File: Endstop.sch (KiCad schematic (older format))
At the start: 4 parts

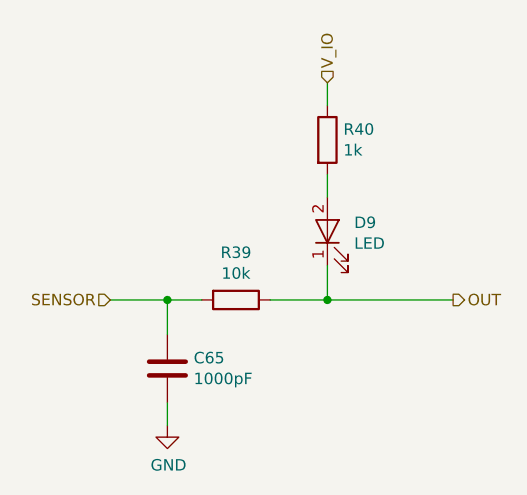
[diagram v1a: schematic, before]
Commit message: Finish the schematics. All pins are assinged to the NUCLEO-64 board.
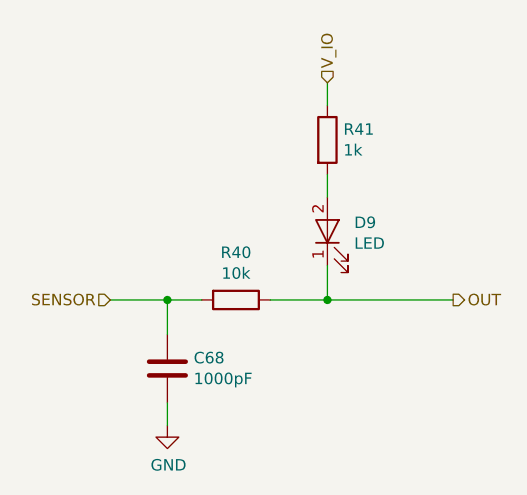
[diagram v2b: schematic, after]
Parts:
- renumbered C12 to C15, R5 to R6, R6 to R7
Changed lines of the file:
@@
 $Descr A4 11693 8268
 encoding utf-8
-Sheet 10 35
+Sheet 5 35
 Title ""
 Date ""
@@
 $EndDescr
 $Comp
-L Device:R R5
+L Device:R R6
 U 1 1 5ACC8647
 P 3950 2850
-AR Path="/5AC337B6/5ACBE919/5AD4BBBB/5ACC8647" Ref="R5"  Part="1"
-AR Path="/5AC337B6/5ACC0AA2/5ACC7E91/5ACC8647" Ref="R15"  Part="1"
-AR Path="/5AC337B6/5ACC0AA2/5ACC8EC2/5ACC8647" Ref="R17"  Part="1"
-AR Path="/5AC337B6/5ACCA309/5ACC7E91/5ACC8647" Ref="R23"  Part="1"
-AR Path="/5AC337B6/5ACCA309/5ACC8EC2/5ACC8647" Ref="R25"  Part="1"
-AR Path="/5AC337B6/5ACE1C6D/5ACC7E91/5ACC8647" Ref="R31"  Part="1"
-AR Path="/5AC337B6/5ACE1C6D/5ACC8EC2/5ACC8647" Ref="R33"  Part="1"
-AR Path="/5AC337B6/5AD9F95A/5AD4BBBB/5ACC8647" Ref="R39"  Part="1"
-F 0 "R39" V 3743 2850 50  0000 C CNN
+AR Path="/5AC337B6/5ACBE919/5AD4BBBB/5ACC8647" Ref="R6"  Part="1"
+AR Path="/5AC337B6/5ACC0AA2/5ACC7E91/5ACC8647" Ref="R16"  Part="1"
+AR Path="/5AC337B6/5ACC0AA2/5ACC8EC2/5ACC8647" Ref="R18"  Part="1"
+AR Path="/5AC337B6/5ACCA309/5ACC7E91/5ACC8647" Ref="R24"  Part="1"
+AR Path="/5AC337B6/5ACCA309/5ACC8EC2/5ACC8647" Ref="R26"  Part="1"
+AR Path="/5AC337B6/5ACE1C6D/5ACC7E91/5ACC8647" Ref="R32"  Part="1"
+AR Path="/5AC337B6/5ACE1C6D/5ACC8EC2/5ACC8647" Ref="R34"  Part="1"
+AR Path="/5AC337B6/5AD9F95A/5AD4BBBB/5ACC8647" Ref="R40"  Part="1"
+F 0 "R40" V 3743 2850 50  0000 C CNN
 F 1 "10k" V 3834 2850 50  0000 C CNN
 F 2 "" V 3880 2850 50  0001 C CNN
@@
 $EndComp
 $Comp
-L Device:R R6
+L Device:R R7
 U 1 1 5ACC864E
 P 4350 2150
-AR Path="/5AC337B6/5ACBE919/5AD4BBBB/5ACC864E" Ref="R6"  Part="1"
-AR Path="/5AC337B6/5ACC0AA2/5ACC7E91/5ACC864E" Ref="R16"  Part="1"
-AR Path="/5AC337B6/5ACC0AA2/5ACC8EC2/5ACC864E" Ref="R18"  Part="1"
-AR Path="/5AC337B6/5ACCA309/5ACC7E91/5ACC864E" Ref="R24"  Part="1"
-AR Path="/5AC337B6/5ACCA309/5ACC8EC2/5ACC864E" Ref="R26"  Part="1"
-AR Path="/5AC337B6/5ACE1C6D/5ACC7E91/5ACC864E" Ref="R32"  Part="1"
-AR Path="/5AC337B6/5ACE1C6D/5ACC8EC2/5ACC864E" Ref="R34"  Part="1"
-AR Path="/5AC337B6/5AD9F95A/5AD4BBBB/5ACC864E" Ref="R40"  Part="1"
-F 0 "R40" H 4420 2196 50  0000 L CNN
+AR Path="/5AC337B6/5ACBE919/5AD4BBBB/5ACC864E" Ref="R7"  Part="1"
+AR Path="/5AC337B6/5ACC0AA2/5ACC7E91/5ACC864E" Ref="R17"  Part="1"
+AR Path="/5AC337B6/5ACC0AA2/5ACC8EC2/5ACC864E" Ref="R19"  Part="1"
+AR Path="/5AC337B6/5ACCA309/5ACC7E91/5ACC864E" Ref="R25"  Part="1"
+AR Path="/5AC337B6/5ACCA309/5ACC8EC2/5ACC864E" Ref="R27"  Part="1"
+AR Path="/5AC337B6/5ACE1C6D/5ACC7E91/5ACC864E" Ref="R33"  Part="1"
+AR Path="/5AC337B6/5ACE1C6D/5ACC8EC2/5ACC864E" Ref="R35"  Part="1"
+AR Path="/5AC337B6/5AD9F95A/5AD4BBBB/5ACC864E" Ref="R41"  Part="1"
+F 0 "R41" H 4420 2196 50  0000 L CNN
 F 1 "1k" H 4420 2105 50  0000 L CNN
 F 2 "" V 4280 2150 50  0001 C CNN
@@
 $EndComp
 $Comp
-L Device:C C12
+L Device:C C15
 U 1 1 5ACC865C
 P 3650 3150
-AR Path="/5AC337B6/5ACBE919/5AD4BBBB/5ACC865C" Ref="C12"  Part="1"
-AR Path="/5AC337B6/5ACC0AA2/5ACC7E91/5ACC865C" Ref="C26"  Part="1"
-AR Path="/5AC337B6/5ACC0AA2/5ACC8EC2/5ACC865C" Ref="C27"  Part="1"
-AR Path="/5AC337B6/5ACCA309/5ACC7E91/5ACC865C" Ref="C39"  Part="1"
-AR Path="/5AC337B6/5ACCA309/5ACC8EC2/5ACC865C" Ref="C40"  Part="1"
-AR Path="/5AC337B6/5ACE1C6D/5ACC7E91/5ACC865C" Ref="C52"  Part="1"
-AR Path="/5AC337B6/5ACE1C6D/5ACC8EC2/5ACC865C" Ref="C53"  Part="1"
-AR Path="/5AC337B6/5AD9F95A/5AD4BBBB/5ACC865C" Ref="C65"  Part="1"
-F 0 "C65" H 3765 3196 50  0000 L CNN
+AR Path="/5AC337B6/5ACBE919/5AD4BBBB/5ACC865C" Ref="C15"  Part="1"
+AR Path="/5AC337B6/5ACC0AA2/5ACC7E91/5ACC865C" Ref="C29"  Part="1"
+AR Path="/5AC337B6/5ACC0AA2/5ACC8EC2/5ACC865C" Ref="C30"  Part="1"
+AR Path="/5AC337B6/5ACCA309/5ACC7E91/5ACC865C" Ref="C42"  Part="1"
+AR Path="/5AC337B6/5ACCA309/5ACC8EC2/5ACC865C" Ref="C43"  Part="1"
+AR Path="/5AC337B6/5ACE1C6D/5ACC7E91/5ACC865C" Ref="C55"  Part="1"
+AR Path="/5AC337B6/5ACE1C6D/5ACC8EC2/5ACC865C" Ref="C56"  Part="1"
+AR Path="/5AC337B6/5AD9F95A/5AD4BBBB/5ACC865C" Ref="C68"  Part="1"
+F 0 "C68" H 3765 3196 50  0000 L CNN
 F 1 "1000pF" H 3765 3105 50  0000 L CNN
 F 2 "" H 3688 3000 50  0001 C CNN
@@
 $EndComp
 $Comp
-L power:GND #PWR09
+L power:GND #PWR019
 U 1 1 5ACC8663
 P 3650 3400
-AR Path="/5AC337B6/5ACBE919/5AD4BBBB/5ACC8663" Ref="#PWR09"  Part="1"
-AR Path="/5AC337B6/5ACC0AA2/5ACC7E91/5ACC8663" Ref="#PWR022"  Part="1"
-AR Path="/5AC337B6/5ACC0AA2/5ACC8EC2/5ACC8663" Ref="#PWR023"  Part="1"
-AR Path="/5AC337B6/5ACCA309/5ACC7E91/5ACC8663" Ref="#PWR033"  Part="1"
-AR Path="/5AC337B6/5ACCA309/5ACC8EC2/5ACC8663" Ref="#PWR034"  Part="1"
-AR Path="/5AC337B6/5ACE1C6D/5ACC7E91/5ACC8663" Ref="#PWR044"  Part="1"
-AR Path="/5AC337B6/5ACE1C6D/5ACC8EC2/5ACC8663" Ref="#PWR045"  Part="1"
-AR Path="/5AC337B6/5AD9F95A/5AD4BBBB/5ACC8663" Ref="#PWR054"  Part="1"
-F 0 "#PWR054" H 3650 3150 50  0001 C CNN
+AR Path="/5AC337B6/5ACBE919/5AD4BBBB/5ACC8663" Ref="#PWR019"  Part="1"
+AR Path="/5AC337B6/5ACC0AA2/5ACC7E91/5ACC8663" Ref="#PWR032"  Part="1"
+AR Path="/5AC337B6/5ACC0AA2/5ACC8EC2/5ACC8663" Ref="#PWR033"  Part="1"
+AR Path="/5AC337B6/5ACCA309/5ACC7E91/5ACC8663" Ref="#PWR043"  Part="1"
+AR Path="/5AC337B6/5ACCA309/5ACC8EC2/5ACC8663" Ref="#PWR044"  Part="1"
+AR Path="/5AC337B6/5ACE1C6D/5ACC7E91/5ACC8663" Ref="#PWR054"  Part="1"
+AR Path="/5AC337B6/5ACE1C6D/5ACC8EC2/5ACC8663" Ref="#PWR055"  Part="1"
+AR Path="/5AC337B6/5AD9F95A/5AD4BBBB/5ACC8663" Ref="#PWR064"  Part="1"
+F 0 "#PWR064" H 3650 3150 50  0001 C CNN
 F 1 "GND" H 3655 3227 50  0000 C CNN
 F 2 "" H 3650 3400 50  0001 C CNN

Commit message: Assigned footprints for all components. Inductors are approximate size. MOSFETs dont agree with the footprints. Saved pcb netlist report as report.txt.
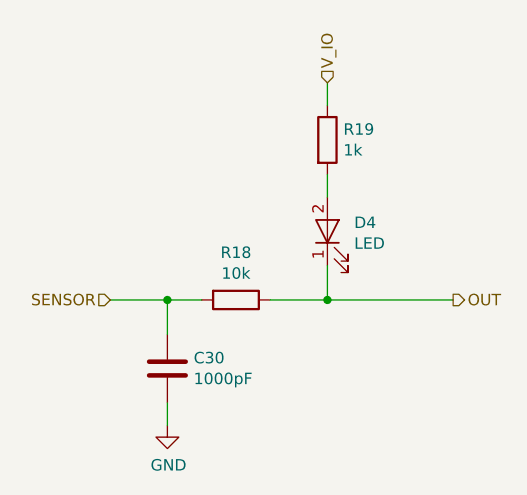
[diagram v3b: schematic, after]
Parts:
- C15: footprint (none) -> Capacitor_SMD:C_0603_1608Metric
- D1: footprint (none) -> LED_SMD:LED_0603_1608Metric
- R6, R7: footprint (none) -> Resistor_SMD:R_0603_1608Metric
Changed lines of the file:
@@
 $Descr A4 11693 8268
 encoding utf-8
-Sheet 5 35
+Sheet 11 35
 Title ""
 Date ""
@@
 AR Path="/5AC337B6/5ACE1C6D/5ACC8EC2/5ACC8647" Ref="R34"  Part="1"
 AR Path="/5AC337B6/5AD9F95A/5AD4BBBB/5ACC8647" Ref="R40"  Part="1"
-F 0 "R40" V 3743 2850 50  0000 C CNN
+F 0 "R18" V 3743 2850 50  0000 C CNN
 F 1 "10k" V 3834 2850 50  0000 C CNN
-F 2 "" V 3880 2850 50  0001 C CNN
+F 2 "Resistor_SMD:R_0603_1608Metric" V 3880 2850 50  0001 C CNN
 F 3 "~" H 3950 2850 50  0001 C CNN
 	1    3950 2850
@@
 AR Path="/5AC337B6/5ACE1C6D/5ACC8EC2/5ACC864E" Ref="R35"  Part="1"
 AR Path="/5AC337B6/5AD9F95A/5AD4BBBB/5ACC864E" Ref="R41"  Part="1"
-F 0 "R41" H 4420 2196 50  0000 L CNN
+F 0 "R19" H 4420 2196 50  0000 L CNN
 F 1 "1k" H 4420 2105 50  0000 L CNN
-F 2 "" V 4280 2150 50  0001 C CNN
+F 2 "Resistor_SMD:R_0603_1608Metric" V 4280 2150 50  0001 C CNN
 F 3 "~" H 4350 2150 50  0001 C CNN
 	1    4350 2150
@@
 AR Path="/5AC337B6/5ACE1C6D/5ACC8EC2/5ACC8655" Ref="D8"  Part="1"
 AR Path="/5AC337B6/5AD9F95A/5AD4BBBB/5ACC8655" Ref="D9"  Part="1"
-F 0 "D9" V 4388 2433 50  0000 R CNN
+F 0 "D4" V 4388 2433 50  0000 R CNN
 F 1 "LED" V 4297 2433 50  0000 R CNN
-F 2 "" H 4350 2550 50  0001 C CNN
+F 2 "LED_SMD:LED_0603_1608Metric" H 4350 2550 50  0001 C CNN
 F 3 "~" H 4350 2550 50  0001 C CNN
 	1    4350 2550
@@
 AR Path="/5AC337B6/5ACE1C6D/5ACC8EC2/5ACC865C" Ref="C56"  Part="1"
 AR Path="/5AC337B6/5AD9F95A/5AD4BBBB/5ACC865C" Ref="C68"  Part="1"
-F 0 "C68" H 3765 3196 50  0000 L CNN
+F 0 "C30" H 3765 3196 50  0000 L CNN
 F 1 "1000pF" H 3765 3105 50  0000 L CNN
-F 2 "" H 3688 3000 50  0001 C CNN
+F 2 "Capacitor_SMD:C_0603_1608Metric" H 3688 3000 50  0001 C CNN
 F 3 "~" H 3650 3150 50  0001 C CNN
 	1    3650 3150

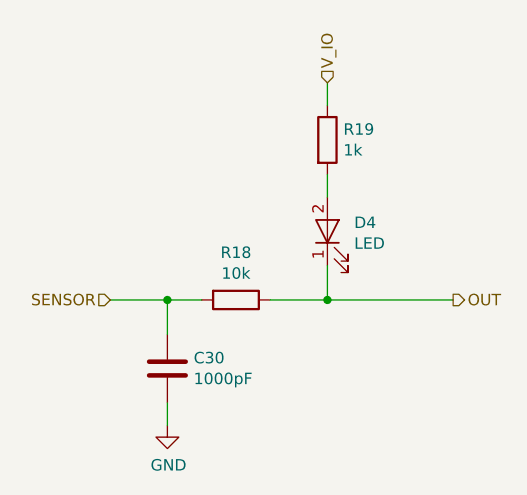
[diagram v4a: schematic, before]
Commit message: Routed most of the power traces.
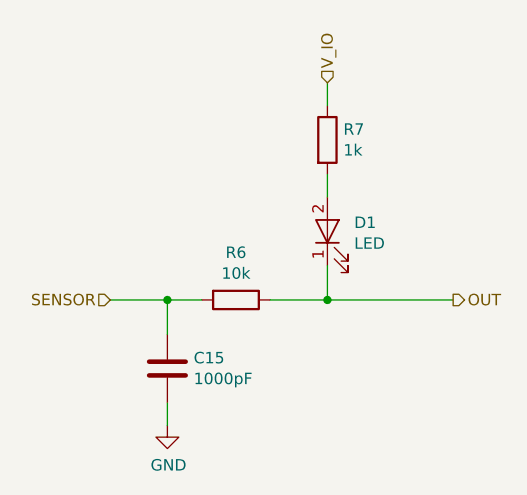
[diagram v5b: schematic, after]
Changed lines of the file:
@@
 AR Path="/5AC337B6/5ACE1C6D/5ACC8EC2/5ACC8647" Ref="R34"  Part="1"
 AR Path="/5AC337B6/5AD9F95A/5AD4BBBB/5ACC8647" Ref="R40"  Part="1"
-F 0 "R18" V 3743 2850 50  0000 C CNN
+F 0 "R6" V 3743 2850 50  0000 C CNN
 F 1 "10k" V 3834 2850 50  0000 C CNN
 F 2 "Resistor_SMD:R_0603_1608Metric" V 3880 2850 50  0001 C CNN
@@
 AR Path="/5AC337B6/5ACE1C6D/5ACC8EC2/5ACC864E" Ref="R35"  Part="1"
 AR Path="/5AC337B6/5AD9F95A/5AD4BBBB/5ACC864E" Ref="R41"  Part="1"
-F 0 "R19" H 4420 2196 50  0000 L CNN
+F 0 "R7" H 4420 2196 50  0000 L CNN
 F 1 "1k" H 4420 2105 50  0000 L CNN
 F 2 "Resistor_SMD:R_0603_1608Metric" V 4280 2150 50  0001 C CNN
@@
 AR Path="/5AC337B6/5ACE1C6D/5ACC8EC2/5ACC8655" Ref="D8"  Part="1"
 AR Path="/5AC337B6/5AD9F95A/5AD4BBBB/5ACC8655" Ref="D9"  Part="1"
-F 0 "D4" V 4388 2433 50  0000 R CNN
+F 0 "D1" V 4388 2433 50  0000 R CNN
 F 1 "LED" V 4297 2433 50  0000 R CNN
 F 2 "LED_SMD:LED_0603_1608Metric" H 4350 2550 50  0001 C CNN
@@
 AR Path="/5AC337B6/5ACE1C6D/5ACC8EC2/5ACC865C" Ref="C56"  Part="1"
 AR Path="/5AC337B6/5AD9F95A/5AD4BBBB/5ACC865C" Ref="C68"  Part="1"
-F 0 "C30" H 3765 3196 50  0000 L CNN
+F 0 "C15" H 3765 3196 50  0000 L CNN
 F 1 "1000pF" H 3765 3105 50  0000 L CNN
 F 2 "Capacitor_SMD:C_0603_1608Metric" H 3688 3000 50  0001 C CNN

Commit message: Added mounting holes and fiducials. Placed all components labels so they are readable.
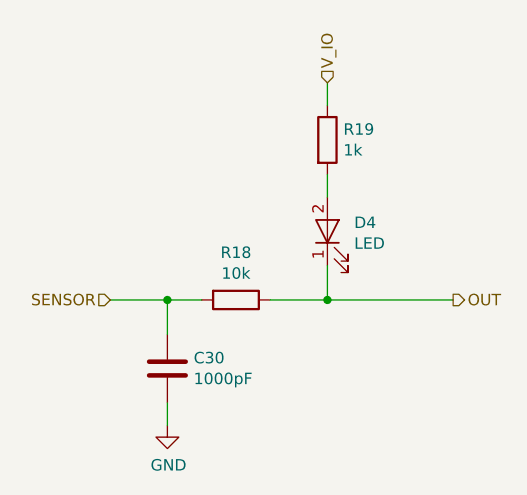
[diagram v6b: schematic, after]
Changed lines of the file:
@@
 AR Path="/5AC337B6/5ACE1C6D/5ACC8EC2/5ACC8647" Ref="R34"  Part="1"
 AR Path="/5AC337B6/5AD9F95A/5AD4BBBB/5ACC8647" Ref="R40"  Part="1"
-F 0 "R6" V 3743 2850 50  0000 C CNN
+F 0 "R18" V 3743 2850 50  0000 C CNN
 F 1 "10k" V 3834 2850 50  0000 C CNN
 F 2 "Resistor_SMD:R_0603_1608Metric" V 3880 2850 50  0001 C CNN
@@
 AR Path="/5AC337B6/5ACE1C6D/5ACC8EC2/5ACC864E" Ref="R35"  Part="1"
 AR Path="/5AC337B6/5AD9F95A/5AD4BBBB/5ACC864E" Ref="R41"  Part="1"
-F 0 "R7" H 4420 2196 50  0000 L CNN
+F 0 "R19" H 4420 2196 50  0000 L CNN
 F 1 "1k" H 4420 2105 50  0000 L CNN
 F 2 "Resistor_SMD:R_0603_1608Metric" V 4280 2150 50  0001 C CNN
@@
 AR Path="/5AC337B6/5ACE1C6D/5ACC8EC2/5ACC8655" Ref="D8"  Part="1"
 AR Path="/5AC337B6/5AD9F95A/5AD4BBBB/5ACC8655" Ref="D9"  Part="1"
-F 0 "D1" V 4388 2433 50  0000 R CNN
+F 0 "D4" V 4388 2433 50  0000 R CNN
 F 1 "LED" V 4297 2433 50  0000 R CNN
 F 2 "LED_SMD:LED_0603_1608Metric" H 4350 2550 50  0001 C CNN
@@
 AR Path="/5AC337B6/5ACE1C6D/5ACC8EC2/5ACC865C" Ref="C56"  Part="1"
 AR Path="/5AC337B6/5AD9F95A/5AD4BBBB/5ACC865C" Ref="C68"  Part="1"
-F 0 "C15" H 3765 3196 50  0000 L CNN
+F 0 "C30" H 3765 3196 50  0000 L CNN
 F 1 "1000pF" H 3765 3105 50  0000 L CNN
 F 2 "Capacitor_SMD:C_0603_1608Metric" H 3688 3000 50  0001 C CNN

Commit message: Update schematics to use TMC5130/TMC2130 drivers.
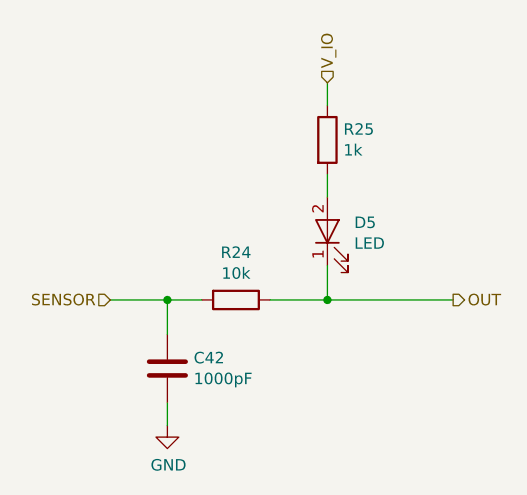
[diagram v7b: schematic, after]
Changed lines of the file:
@@
 AR Path="/5AC337B6/5ACE1C6D/5ACC8EC2/5ACC8647" Ref="R34"  Part="1"
 AR Path="/5AC337B6/5AD9F95A/5AD4BBBB/5ACC8647" Ref="R40"  Part="1"
-F 0 "R18" V 3743 2850 50  0000 C CNN
+F 0 "R24" V 3743 2850 50  0000 C CNN
 F 1 "10k" V 3834 2850 50  0000 C CNN
 F 2 "Resistor_SMD:R_0603_1608Metric" V 3880 2850 50  0001 C CNN
@@
 AR Path="/5AC337B6/5ACE1C6D/5ACC8EC2/5ACC864E" Ref="R35"  Part="1"
 AR Path="/5AC337B6/5AD9F95A/5AD4BBBB/5ACC864E" Ref="R41"  Part="1"
-F 0 "R19" H 4420 2196 50  0000 L CNN
+F 0 "R25" H 4420 2196 50  0000 L CNN
 F 1 "1k" H 4420 2105 50  0000 L CNN
 F 2 "Resistor_SMD:R_0603_1608Metric" V 4280 2150 50  0001 C CNN
@@
 AR Path="/5AC337B6/5ACE1C6D/5ACC8EC2/5ACC8655" Ref="D8"  Part="1"
 AR Path="/5AC337B6/5AD9F95A/5AD4BBBB/5ACC8655" Ref="D9"  Part="1"
-F 0 "D4" V 4388 2433 50  0000 R CNN
+F 0 "D5" V 4388 2433 50  0000 R CNN
 F 1 "LED" V 4297 2433 50  0000 R CNN
 F 2 "LED_SMD:LED_0603_1608Metric" H 4350 2550 50  0001 C CNN
@@
 AR Path="/5AC337B6/5ACE1C6D/5ACC8EC2/5ACC865C" Ref="C56"  Part="1"
 AR Path="/5AC337B6/5AD9F95A/5AD4BBBB/5ACC865C" Ref="C68"  Part="1"
-F 0 "C30" H 3765 3196 50  0000 L CNN
+F 0 "C42" H 3765 3196 50  0000 L CNN
 F 1 "1000pF" H 3765 3105 50  0000 L CNN
 F 2 "Capacitor_SMD:C_0603_1608Metric" H 3688 3000 50  0001 C CNN

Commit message: Added motor clock source.
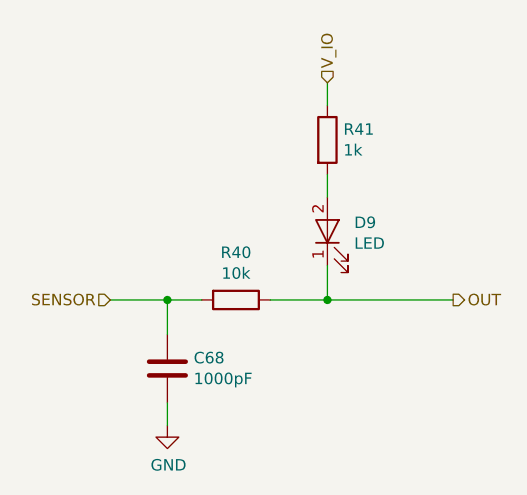
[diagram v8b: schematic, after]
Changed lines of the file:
@@
 AR Path="/5AC337B6/5ACE1C6D/5ACC8EC2/5ACC8647" Ref="R34"  Part="1"
 AR Path="/5AC337B6/5AD9F95A/5AD4BBBB/5ACC8647" Ref="R40"  Part="1"
-F 0 "R24" V 3743 2850 50  0000 C CNN
+F 0 "R40" V 3743 2850 50  0000 C CNN
 F 1 "10k" V 3834 2850 50  0000 C CNN
 F 2 "Resistor_SMD:R_0603_1608Metric" V 3880 2850 50  0001 C CNN
@@
 AR Path="/5AC337B6/5ACE1C6D/5ACC8EC2/5ACC864E" Ref="R35"  Part="1"
 AR Path="/5AC337B6/5AD9F95A/5AD4BBBB/5ACC864E" Ref="R41"  Part="1"
-F 0 "R25" H 4420 2196 50  0000 L CNN
+F 0 "R41" H 4420 2196 50  0000 L CNN
 F 1 "1k" H 4420 2105 50  0000 L CNN
 F 2 "Resistor_SMD:R_0603_1608Metric" V 4280 2150 50  0001 C CNN
@@
 AR Path="/5AC337B6/5ACE1C6D/5ACC8EC2/5ACC8655" Ref="D8"  Part="1"
 AR Path="/5AC337B6/5AD9F95A/5AD4BBBB/5ACC8655" Ref="D9"  Part="1"
-F 0 "D5" V 4388 2433 50  0000 R CNN
+F 0 "D9" V 4388 2433 50  0000 R CNN
 F 1 "LED" V 4297 2433 50  0000 R CNN
 F 2 "LED_SMD:LED_0603_1608Metric" H 4350 2550 50  0001 C CNN
@@
 AR Path="/5AC337B6/5ACE1C6D/5ACC8EC2/5ACC865C" Ref="C56"  Part="1"
 AR Path="/5AC337B6/5AD9F95A/5AD4BBBB/5ACC865C" Ref="C68"  Part="1"
-F 0 "C42" H 3765 3196 50  0000 L CNN
+F 0 "C68" H 3765 3196 50  0000 L CNN
 F 1 "1000pF" H 3765 3105 50  0000 L CNN
 F 2 "Capacitor_SMD:C_0603_1608Metric" H 3688 3000 50  0001 C CNN
